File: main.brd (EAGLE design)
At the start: 100 x 50 mm, 101 parts, among them IC1 LD1117S50TR, IC2 LD398533RM, IC3 CP2102, IC4 PM8834-SO08N, IC5 PM8834-SO08N, J1 RJ11, Q10 IRF3205SPBF, Q11 IRF3205SPBF, Q12 IRF3205SPBF, Q13 IRF3205SPBF, Q2 BSS138, Q3 BSS138, Q6 BSS138, Q7 BSS138, Q8 BSS138, Q9 BSS138, T1 SS8050-G, T2 SS8050-G, U1 ESP-WROOM-32, U2 TMP275AIDR, U3 TSL2561T, X1 1751248, X2 1751280, X3 1751277

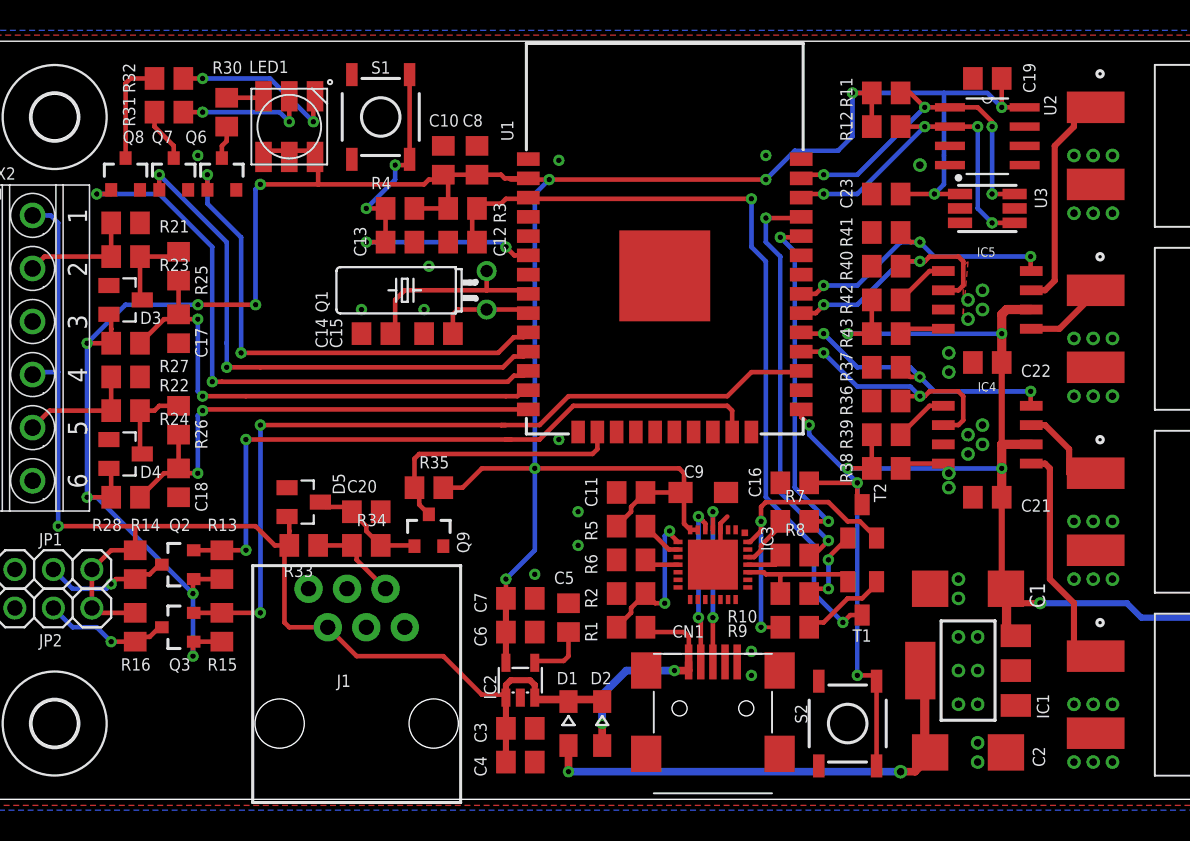
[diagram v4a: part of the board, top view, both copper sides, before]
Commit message: Replaced usb chip by connector
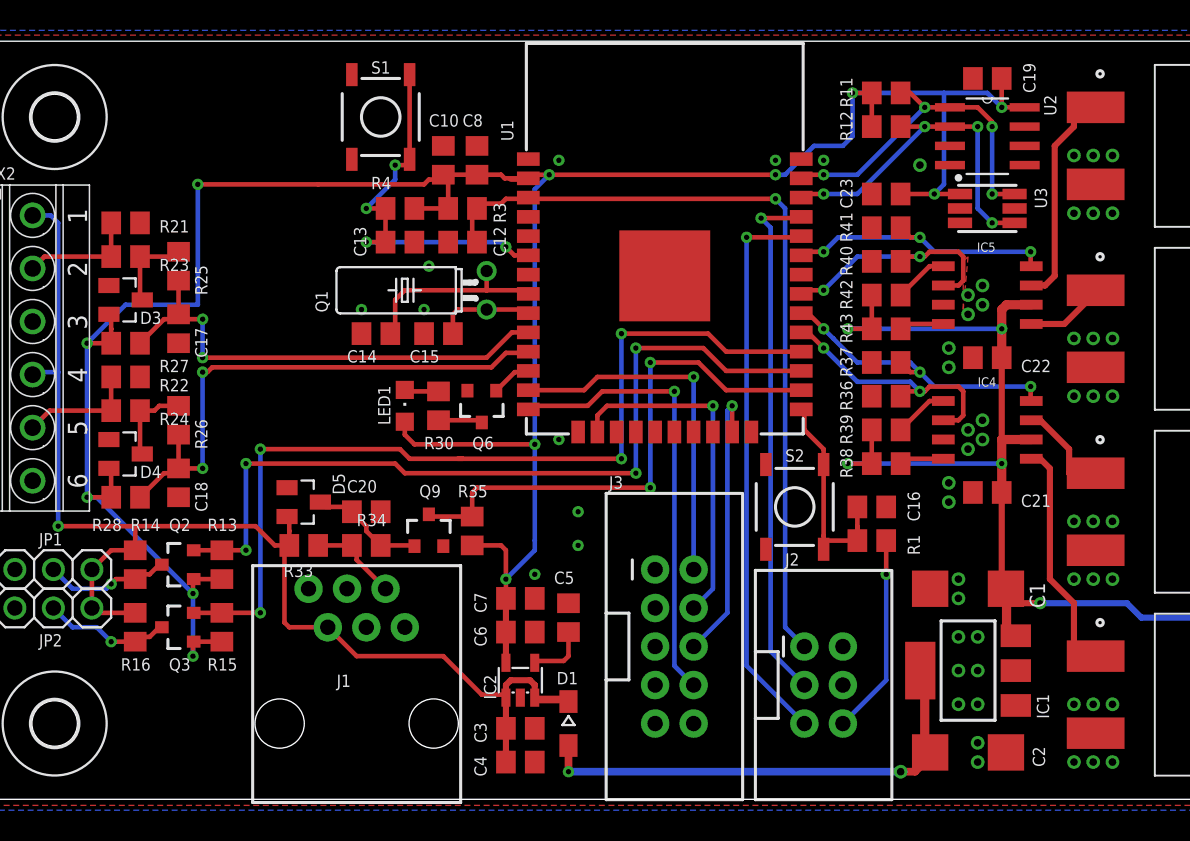
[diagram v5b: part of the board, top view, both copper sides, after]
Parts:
- removed C11: 100nF, resistor:C0805
- removed C9: (no value), resistor:SMC_A
- removed CN1: (no value), adafruit:USB-MINIB
- removed D2: BAT60JFILM, diode:SOD323-W
- removed IC3: CP2102, silabs:MLP28
- removed Q7, Q8: BSS138, SparkFun:SOT23-3
- removed R10, R31, R32, R6, R9: 10K, resistor:R0805
- removed R2: 47K5, resistor:R0805
- removed R5: 2K, resistor:R0805
- removed R7, R8: 0R, resistor:R0805
- removed T1, T2: SS8050-G, transistor:SOT23-BEC
- added J2: (no value), SparkFun-Connectors:2X3-SHROUDED
- added J3: (no value), SparkFun-Connectors:2X5-SHROUDED
- LED1: value RGBLED5050 -> RED; device adafruit:RGBLED5050 -> led:CHIPLED_0805
- R1: value 22K1 -> 10K
- R3, R4: value 1K -> 10K
- R30: value 10K -> 1K
- moved R30 23.9 mm to (-19.7, 0.95)
- moved Q6 22.9 mm to (-16.8, 0.95), turned to 180 degrees
- moved LED1 19.9 mm to (-21.9, 0.95), turned to 0 degrees
- moved R1 16.9 mm to (8.89, -7.94)
- moved S2 14.7 mm to (3.81, -5.71)
- moved C16 5.32 mm to (8.89, -5.71), turned to 0 degrees
- moved R35 4.04 mm to (-17.5, -7.30), turned to 270 degrees
- moved IC5 0.32 mm to (16.5, 8.26)
- moved R42 0.32 mm to (9.84, 8.26)
- moved C22 0.32 mm to (16.5, 4.13)
- moved IC4 0.32 mm to (16.5, -0.64)
- moved R39 0.32 mm to (9.84, -0.64)
- moved C21 0.32 mm to (16.5, -4.76)
- moved R36 0.32 mm to (9.84, 1.59)
- moved R37 0.32 mm to (9.84, 3.81)
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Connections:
- removed net CTS: IC3.23
- removed net DCD: IC3.1
- removed net DSR: IC3.27
- removed net DTR: IC3.28, R9.1, T2.E
- removed net EN: C12.1, R3.1, T1.C, U1.3
- removed net IO0: C16.1, S2.3, S2.4, T2.C, U1.25
- removed net LEDB: Q8.1, U1.12
- removed net LEDG: Q7.1, U1.11
- removed net N$11: LED1.5, R31.1
- removed net N$19: IC3.11, R6.1
- removed net N$21: IC3.9, R5.1
- removed net N$24: IC3.8, R1.2, R2.2
- removed net N$25: CN1.D-, IC3.5
- removed net N$29: LED1.4, R32.1
- removed net N$31: Q7.3, R31.2
- removed net N$32: Q8.3, R32.2
- removed net N$42: R9.2, T1.B
- removed net N$43: R10.2, T2.B
- removed net N$6: CN1.D+, IC3.4
- removed net RI: IC3.2
- removed net RTS: IC3.24, R10.1, T1.E
- removed net RXD: IC3.25, R8.1
- removed net RXD0: R7.2, U1.34
- removed net TXD: IC3.26, R7.1
- removed net TXD0: R8.2, U1.35
- removed net VBUS: CN1.VBUS, D2.A, R1.1
- new net ESP_EN: C12.1, J2.1, R3.1, U1.3
- new net ESP_IO0: C16.1, R1.2, S2.3, S2.4, U1.25
- new net ESP_RXD0: J2.5, U1.34
- new net ESP_TCK: J3.4, U1.16
- new net ESP_TDI: J3.8, U1.14
- new net ESP_TDO: J3.6, U1.23
- new net ESP_TMS: J3.2, U1.13
- new net ESP_TXD0: J2.3, U1.35
- new net N$4: J2.6, R1.1
- net +3V3: now also J2.2, J3.1, LED1.A; no longer C11.1, C9.+, IC3.6, IC3.7, LED1.1, LED1.2, LED1.3, R5.2
- net +5V: no longer D2.C
- net GND: now also J2.4, J3.3, J3.5, J3.7, J3.9; no longer C11.2, C9.-, CN1.GND, IC3.3, IC3.EXP, IC3.M, Q7.2, Q8.2, R2.1, R6.2
- net INP1: now also U1.10; no longer U1.13
- net INP2: now also U1.11; no longer U1.14
- net LEDR: now also U1.12; no longer U1.10
- net LV0: now also U1.27; no longer U1.23
- net LV1: now also U1.28; no longer U1.27
- net N$5: now also LED1.C; no longer LED1.6
- net P1: now also U1.26; no longer U1.16
- net PWM0: now also U1.29; no longer U1.28
- net PWM1: now also U1.30; no longer U1.29
- net PWM2: now also U1.31; no longer U1.30
- net PWM3: now also U1.33; no longer U1.31
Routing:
- net EN: track 53.0 -> 0.00 mm, vias 2 -> 0
- net ESP_EN: track 0.00 -> 53.0 mm, vias 0 -> 1
- net LEDB: track 40.3 -> 0.00 mm, vias 2 -> 0
- net ESP_RXD0: track 0.00 -> 37.3 mm, vias 0 -> 1
- net LEDG: track 35.9 -> 0.00 mm, vias 2 -> 0
- net ESP_TXD0: track 0.00 -> 34.7 mm, vias 0 -> 1
- net IO0: track 31.1 -> 0.00 mm, vias 3 -> 0
- net LEDR: track 33.2 -> 2.65 mm, vias 2 -> 0
- net ESP_TDI: track 0.00 -> 30.0 mm, vias 0 -> 1
- net TXD0: track 27.0 -> 0.00 mm, vias 2 -> 0
- net ESP_TMS: track 0.00 -> 24.0 mm, vias 0 -> 1
- net ESP_TCK: track 0.00 -> 22.8 mm, vias 0 -> 1
- net RXD0: track 22.7 -> 0.00 mm, vias 2 -> 0
- net DTR: track 19.7 -> 0.00 mm, vias 2 -> 0
- net ESP_TDO: track 0.00 -> 18.7 mm, vias 0 -> 1
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
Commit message: work on programmer board
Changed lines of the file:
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@@
 <wire x1="17.4625" y1="-4.76375" x2="17.4625" y2="-10.835" width="0.4064" layer="1"/>
 <wire x1="17.74" y1="-11.1125" x2="17.4625" y2="-10.835" width="0.4064" layer="1"/>
-<wire x1="46.455" y1="-12.8625" x2="45.5575" y2="-12.8625" width="0.4064" layer="16"/>
-<wire x1="45.5575" y1="-12.8625" x2="45.085" y2="-13.335" width="0.4064" layer="16"/>
+<wire x1="46.455" y1="-12.8625" x2="45.5575" y2="-12.8625" width="0.508" layer="16"/>
+<wire x1="45.5575" y1="-12.8625" x2="45.085" y2="-13.335" width="0.508" layer="16"/>
 <wire x1="45.085" y1="-13.335" x2="45.085" y2="-13.0175" width="0.4064" layer="16"/>
-<wire x1="26.67" y1="-13.0175" x2="25.7175" y2="-12.065" width="0.4064" layer="16"/>
-<wire x1="25.7175" y1="-12.065" x2="20.0025" y2="-12.065" width="0.4064" layer="16"/>
-<wire x1="45.085" y1="-13.0175" x2="26.67" y2="-13.0175" width="0.4064" layer="16"/>
+<wire x1="26.67" y1="-13.0175" x2="25.7175" y2="-12.065" width="0.508" layer="16"/>
+<wire x1="25.7175" y1="-12.065" x2="20.0025" y2="-12.065" width="0.508" layer="16"/>
+<wire x1="45.085" y1="-13.0175" x2="26.67" y2="-13.0175" width="0.508" layer="16"/>
 <via x="20.0025" y="-12.065" extent="1-16" drill="0.4"/>
-<wire x1="20.0025" y1="-12.065" x2="17.78" y2="-12.065" width="0.4064" layer="1"/>
+<wire x1="20.0025" y1="-12.065" x2="17.78" y2="-12.065" width="0.508" layer="1"/>
 <wire x1="7.305" y1="-2.855" x2="7.3025" y2="-2.8575" width="0.3048" layer="1"/>
 <via x="7.3025" y="-2.8575" extent="1-16" drill="0.35"/>
